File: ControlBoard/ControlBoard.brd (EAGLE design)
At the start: 100 x 80 mm, 7 parts, among them J1 FTDI_DEVICE

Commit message: updates to control board...needs more work
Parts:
- moved R1 112.0 mm to (40.6, 55.9)
- moved C1 105.2 mm to (44.5, 30.5)
- moved J1 104.2 mm to (69.8, 45.7), turned to 270 degrees
- moved R2 100.5 mm to (15.2, 45.7)
- moved S1 100.0 mm to (26.7, 47.0)
- moved X1 73.9 mm to (53.3, 49.5)
- moved JP1 67.1 mm to (33.0, 45.7), turned to 90 degrees
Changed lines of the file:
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@@
 </autorouter>
 <elements>
-<element name="X1" library="adafruit" package="ESP-12" value="" x="-11.43" y="13.97"/>
-<element name="JP1" library="adafruit" package="1X06" value="" x="-7.62" y="-7.62"/>
-<element name="J1" library="quad" package="FTDI_DEVICE_SIDE" value="FTDI_DEVICE" x="-6.35" y="-25.4"/>
-<element name="R1" library="rcl" package="R0603" value="10K" x="-20.32" y="-38.1"/>
-<element name="S1" library="quad" package="TACTILE-SWITCH-SMD" value="SWITCH-MOMENTARY-2SMD" x="-16.51" y="-43.18">
-<attribute name="PROD_ID" value="SWCH-08247" x="-16.51" y="-43.18" size="1.778" layer="27" display="off"/>
+<element name="X1" library="adafruit" package="ESP-12" value="" x="53.34" y="49.53"/>
+<element name="JP1" library="adafruit" package="1X06" value="" x="33.02" y="45.72" rot="R90"/>
+<element name="J1" library="quad" package="FTDI_DEVICE_SIDE" value="FTDI_DEVICE" x="69.85" y="45.72" rot="R270"/>
+<element name="R1" library="rcl" package="R0603" value="10K" x="40.64" y="55.88"/>
+<element name="S1" library="quad" package="TACTILE-SWITCH-SMD" value="SWITCH-MOMENTARY-2SMD" x="26.67" y="46.99">
+<attribute name="PROD_ID" value="SWCH-08247" x="26.67" y="46.99" size="1.778" layer="27" display="off"/>
 </element>
-<element name="R2" library="rcl" package="R0603" value="10K" x="-20.32" y="-48.26"/>
-<element name="C1" library="rcl" package="C0603" value="100nF" x="-19.05" y="-53.34"/>
+<element name="R2" library="rcl" package="R0603" value="10K" x="15.24" y="45.72"/>
+<element name="C1" library="rcl" package="C0603" value="100nF" x="44.45" y="30.48"/>
 </elements>
 <signals>
@@
 <contactref element="JP1" pad="3"/>
 <contactref element="S1" pad="3"/>
-<wire x1="-8.89" y1="-7.62" x2="-19.304" y2="-45.085" width="0" layer="19" extent="1-1"/>
-<wire x1="-3.93" y1="4.47" x2="-8.89" y2="-7.62" width="0" layer="19" extent="1-1"/>
+<wire x1="33.02" y1="44.45" x2="60.84" y2="40.03" width="0" layer="19" extent="1-1"/>
+<wire x1="23.876" y1="45.085" x2="33.02" y2="44.45" width="0" layer="19" extent="1-1"/>
 </signal>
 <signal name="SCK">
 <contactref element="X1" pad="5"/>
 <contactref element="JP1" pad="6"/>
-<wire x1="-1.27" y1="-7.62" x2="-18.93" y2="10.47" width="0" layer="19" extent="1-1"/>
+<wire x1="33.02" y1="52.07" x2="45.84" y2="46.03" width="0" layer="19" extent="1-1"/>
 </signal>
 <signal name="MISO">
 <contactref element="X1" pad="6"/>
 <contactref element="JP1" pad="4"/>
-<wire x1="-18.93" y1="8.47" x2="-6.35" y2="-7.62" width="0" layer="19" extent="1-1"/>
+<wire x1="33.02" y1="46.99" x2="45.84" y2="44.03" width="0" layer="19" extent="1-1"/>
 </signal>
 <signal name="CS">
 <contactref element="X1" pad="12"/>
 <contactref element="JP1" pad="5"/>
-<wire x1="-3.93" y1="10.47" x2="-3.81" y2="-7.62" width="0" layer="19" extent="1-1"/>
+<wire x1="33.02" y1="49.53" x2="60.84" y2="46.03" width="0" layer="19" extent="1-1"/>
 </signal>
 <signal name="TX">
 <contactref element="J1" pad="P$2"/>
 <contactref element="X1" pad="16"/>
-<wire x1="-3.93" y1="18.47" x2="-10.16" y2="-25.4" width="0" layer="19" extent="1-1"/>
+<wire x1="60.84" y1="54.03" x2="69.85" y2="49.53" width="0" layer="19" extent="1-1"/>
 </signal>
 <signal name="RX">
 <contactref element="J1" pad="P$3"/>
 <contactref element="X1" pad="15"/>
-<wire x1="-3.93" y1="16.47" x2="-7.62" y2="-25.4" width="0" layer="19" extent="1-1"/>
+<wire x1="60.84" y1="52.03" x2="69.85" y2="46.99" width="0" layer="19" extent="1-1"/>
 </signal>
 <signal name="N$1">
 <contactref element="J1" pad="P$5"/>
 <contactref element="J1" pad="P$6"/>
-<wire x1="0" y1="-25.4" x2="-2.54" y2="-25.4" width="0" layer="19" extent="1-1"/>
+<wire x1="69.85" y1="39.37" x2="69.85" y2="41.91" width="0" layer="19" extent="1-1"/>
 </signal>
 <signal name="DTR">
 <contactref element="J1" pad="P$1"/>
 <contactref element="C1" pad="2"/>
-<wire x1="-12.7" y1="-25.4" x2="-18.2" y2="-53.34" width="0" layer="19" extent="1-1"/>
+<wire x1="45.3" y1="30.48" x2="69.85" y2="52.07" width="0" layer="19" extent="1-1"/>
 </signal>
 <signal name="3V3">
@@
 <contactref element="JP1" pad="1"/>
 <contactref element="R2" pad="2"/>
-<wire x1="-21.17" y1="-38.1" x2="-19.47" y2="-48.26" width="0" layer="19" extent="1-1"/>
-<wire x1="-5.08" y1="-25.4" x2="-21.17" y2="-38.1" width="0" layer="19" extent="1-1"/>
-<wire x1="-13.97" y1="-7.62" x2="-5.08" y2="-25.4" width="0" layer="19" extent="1-1"/>
-<wire x1="-18.93" y1="4.47" x2="-13.97" y2="-7.62" width="0" layer="19" extent="1-1"/>
+<wire x1="45.84" y1="40.03" x2="69.85" y2="44.45" width="0" layer="19" extent="1-1"/>
+<wire x1="33.02" y1="39.37" x2="45.84" y2="40.03" width="0" layer="19" extent="1-1"/>
+<wire x1="39.79" y1="55.88" x2="45.84" y2="40.03" width="0" layer="19" extent="1-1"/>
+<wire x1="16.09" y1="45.72" x2="33.02" y2="39.37" width="0" layer="19" extent="1-1"/>
 </signal>
 <signal name="CH_PD">
 <contactref element="R1" pad="2"/>
 <contactref element="X1" pad="3"/>
-<wire x1="-18.93" y1="14.47" x2="-19.47" y2="-38.1" width="0" layer="19" extent="1-1"/>
+<wire x1="45.84" y1="50.03" x2="41.49" y2="55.88" width="0" layer="19" extent="1-1"/>
 </signal>
 <signal name="RST">
@@
 <contactref element="R2" pad="1"/>
 <contactref element="C1" pad="1"/>
-<wire x1="-21.17" y1="-48.26" x2="-19.9" y2="-53.34" width="0" layer="19" extent="1-1"/>
-<wire x1="-19.304" y1="-41.275" x2="-21.17" y2="-48.26" width="0" layer="19" extent="1-1"/>
-<wire x1="-18.93" y1="18.47" x2="-19.304" y2="-41.275" width="0" layer="19" extent="1-1"/>
+<wire x1="23.876" y1="48.895" x2="45.84" y2="54.03" width="0" layer="19" extent="1-1"/>
+<wire x1="14.39" y1="45.72" x2="23.876" y2="48.895" width="0" layer="19" extent="1-1"/>
+<wire x1="43.6" y1="30.48" x2="45.84" y2="54.03" width="0" layer="19" extent="1-1"/>
 </signal>
 </signals>

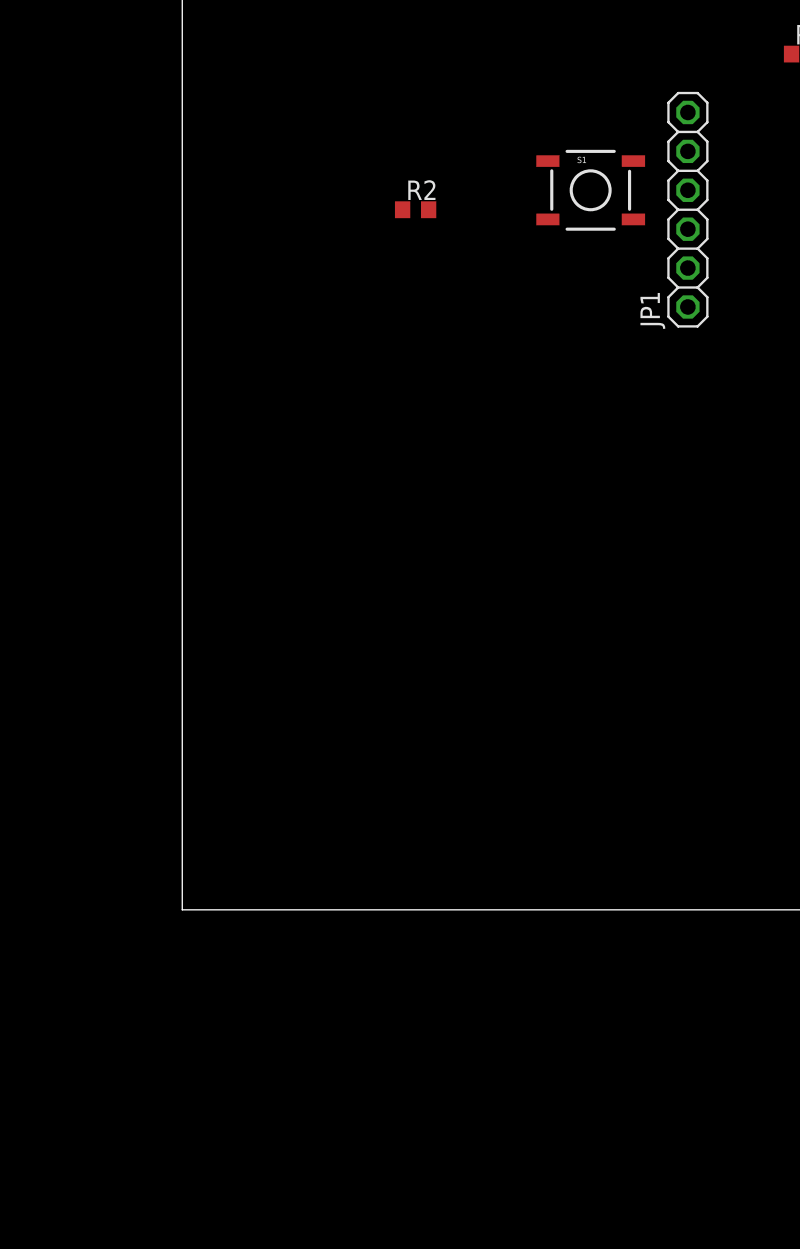
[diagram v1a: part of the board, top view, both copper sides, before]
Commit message: added thermocouple-digital chip
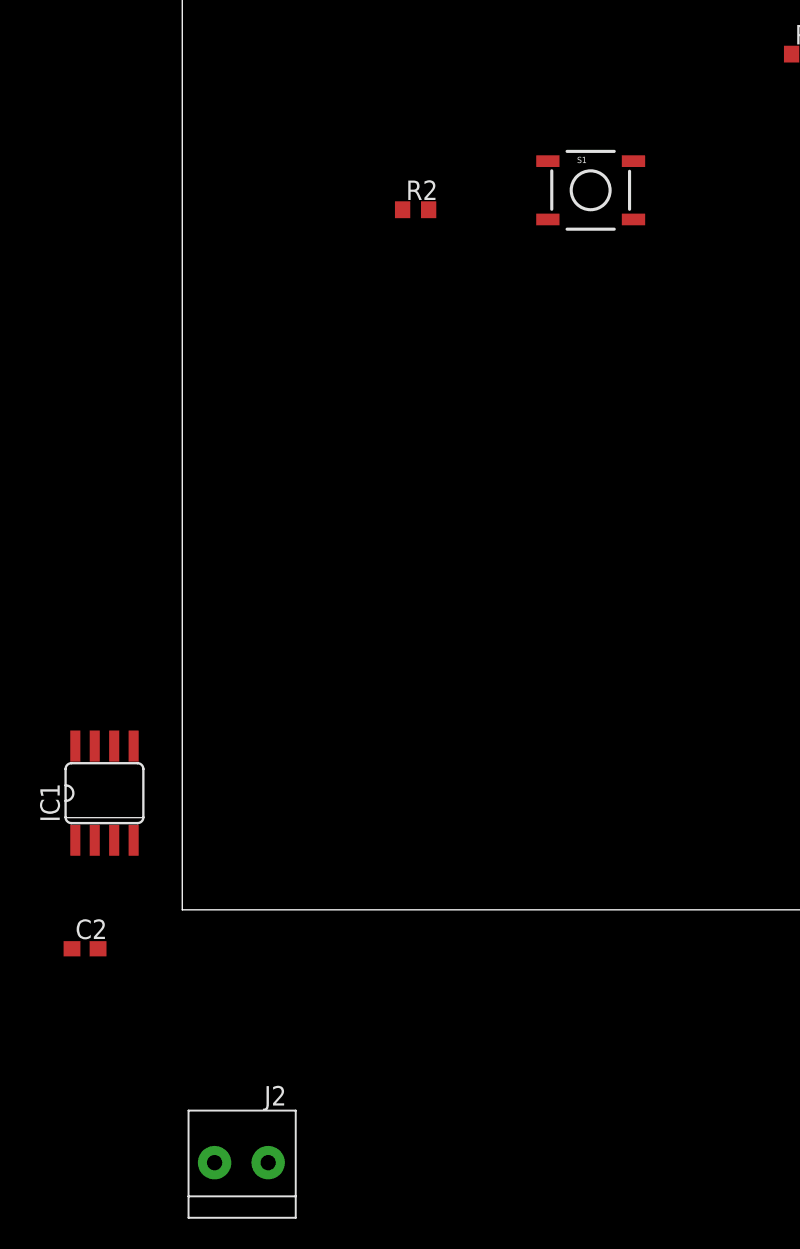
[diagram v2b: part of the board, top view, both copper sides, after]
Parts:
- removed JP1: (no value), adafruit:1X06
- added C2: 100nF, rcl:C0603
- added IC1: MAX6675, adafruit:SO08
- added J2: 1X2-3.5MM, adafruit:1X2-3.5MM
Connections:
- new net T+: C2.1, IC1.3, J2.1
- new net T-: C2.2, IC1.2, J2.2
- net 3V3: now also IC1.4; no longer JP1.1
- net CS: now also IC1.6; no longer JP1.5
- net GND: now also IC1.1; no longer JP1.3
- net MISO: now also IC1.7; no longer JP1.4
- net SCK: now also IC1.5; no longer JP1.6
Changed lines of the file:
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@@
 <elements>
 <element name="X1" library="adafruit" package="ESP-12" value="" x="53.34" y="49.53"/>
-<element name="JP1" library="adafruit" package="1X06" value="" x="33.02" y="45.72" rot="R90"/>
 <element name="J1" library="quad" package="FTDI_DEVICE_SIDE" value="FTDI_DEVICE" x="69.85" y="45.72" rot="R270"/>
 <element name="R1" library="rcl" package="R0603" value="10K" x="40.64" y="55.88"/>
@@
 <element name="R2" library="rcl" package="R0603" value="10K" x="15.24" y="45.72"/>
 <element name="C1" library="rcl" package="C0603" value="100nF" x="44.45" y="30.48"/>
+<element name="IC1" library="adafruit" package="SO08" value="MAX6675" x="-5.08" y="7.62"/>
+<element name="C2" library="rcl" package="C0603" value="100nF" x="-6.35" y="-2.54"/>
+<element name="J2" library="adafruit" package="1X2-3.5MM" value="1X2-3.5MM" x="3.81" y="-16.51"/>
 </elements>
 <signals>
 <signal name="GND">
 <contactref element="X1" pad="9"/>
-<contactref element="JP1" pad="3"/>
 <contactref element="S1" pad="3"/>
-<wire x1="33.02" y1="44.45" x2="60.84" y2="40.03" width="0" layer="19" extent="1-1"/>
-<wire x1="23.876" y1="45.085" x2="33.02" y2="44.45" width="0" layer="19" extent="1-1"/>
+<contactref element="IC1" pad="1"/>
+<wire x1="23.876" y1="45.085" x2="60.84" y2="40.03" width="0" layer="19" extent="1-1"/>
+<wire x1="-6.985" y1="4.5466" x2="23.876" y2="45.085" width="0" layer="19" extent="1-1"/>
 </signal>
 <signal name="SCK">
 <contactref element="X1" pad="5"/>
-<contactref element="JP1" pad="6"/>
-<wire x1="33.02" y1="52.07" x2="45.84" y2="46.03" width="0" layer="19" extent="1-1"/>
+<contactref element="IC1" pad="5"/>
+<wire x1="-3.175" y1="10.6934" x2="45.84" y2="46.03" width="0" layer="19" extent="1-1"/>
 </signal>
 <signal name="MISO">
 <contactref element="X1" pad="6"/>
-<contactref element="JP1" pad="4"/>
-<wire x1="33.02" y1="46.99" x2="45.84" y2="44.03" width="0" layer="19" extent="1-1"/>
+<contactref element="IC1" pad="7"/>
+<wire x1="-5.715" y1="10.6934" x2="45.84" y2="44.03" width="0" layer="19" extent="1-1"/>
 </signal>
 <signal name="CS">
 <contactref element="X1" pad="12"/>
-<contactref element="JP1" pad="5"/>
-<wire x1="33.02" y1="49.53" x2="60.84" y2="46.03" width="0" layer="19" extent="1-1"/>
+<contactref element="IC1" pad="6"/>
+<wire x1="-4.445" y1="10.6934" x2="60.84" y2="46.03" width="0" layer="19" extent="1-1"/>
 </signal>
 <signal name="TX">
@@
 <contactref element="X1" pad="8"/>
 <contactref element="R1" pad="1"/>
-<contactref element="JP1" pad="1"/>
 <contactref element="R2" pad="2"/>
+<contactref element="IC1" pad="4"/>
 <wire x1="45.84" y1="40.03" x2="69.85" y2="44.45" width="0" layer="19" extent="1-1"/>
-<wire x1="33.02" y1="39.37" x2="45.84" y2="40.03" width="0" layer="19" extent="1-1"/>
 <wire x1="39.79" y1="55.88" x2="45.84" y2="40.03" width="0" layer="19" extent="1-1"/>
-<wire x1="16.09" y1="45.72" x2="33.02" y2="39.37" width="0" layer="19" extent="1-1"/>
+<wire x1="16.09" y1="45.72" x2="39.79" y2="55.88" width="0" layer="19" extent="1-1"/>
+<wire x1="-3.175" y1="4.5466" x2="16.09" y2="45.72" width="0" layer="19" extent="1-1"/>
 </signal>
 <signal name="CH_PD">
@@
 <wire x1="43.6" y1="30.48" x2="45.84" y2="54.03" width="0" layer="19" extent="1-1"/>
 </signal>
+<signal name="T-">
+<contactref element="C2" pad="2"/>
+<contactref element="IC1" pad="2"/>
+<contactref element="J2" pad="2"/>
+<wire x1="-5.5" y1="-2.54" x2="2.11" y2="-16.51" width="0" layer="19" extent="1-1"/>
+<wire x1="-5.715" y1="4.5466" x2="-5.5" y2="-2.54" width="0" layer="19" extent="1-1"/>
+</signal>
+<signal name="T+">
+<contactref element="IC1" pad="3"/>
+<contactref element="C2" pad="1"/>
+<contactref element="J2" pad="1"/>
+<wire x1="-7.2" y1="-2.54" x2="5.61" y2="-16.51" width="0" layer="19" extent="1-1"/>
+<wire x1="-4.445" y1="4.5466" x2="-7.2" y2="-2.54" width="0" layer="19" extent="1-1"/>
+</signal>
 </signals>

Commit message: updated eagle board and schematic files
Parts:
- added C3, C4: 1uF, rcl:C0603
- added J3: 1X2-3.5MM, adafruit:1X2-3.5MM
- added MCP1802T-3302I/OT: (no value), quad:SOT95P270X145-5N
- added T1: 2N4401, transistor:TO92-EBC
- added X2: MINI-USB-32005-201, con-cypressindustries:32005-201
- moved R1 47.3 mm to (19.7, 13.5)
- moved J1 44.6 mm to (42.8, 10.2)
- moved X1 43.1 mm to (30.5, 13.0)
- moved S1 35.0 mm to (13.9, 14.4), turned to 180 degrees
- moved R2 30.0 mm to (19.7, 16.0), turned to 180 degrees
- moved C1 26.5 mm to (20.7, 18.8), turned to 90 degrees
- moved J2 24.0 mm to (6.38, 7.39), turned to 270 degrees
- moved IC1 19.4 mm to (14.3, 7.42), turned to 270 degrees
- moved C2 18.0 mm to (8.71, 7.37), flipped to the bottom, turned to 90 degrees
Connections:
- net T+ renamed THERMOCOUPLE+
- net T- renamed THERMOCOUPLE-
- removed net N$1: J1.P$5, J1.P$6
- new net 5V: C3.1, MCP1802T-3302I/OT.1, MCP1802T-3302I/OT.3, T1.C, X2.1
- new net CTS: J1.P$5, X1.7
- new net RELAY_COIL: J3.1, T1.E
- new net RELAY_CTRL: T1.B, X1.14
- net 3V3: now also C4.1, MCP1802T-3302I/OT.5
- net CS: now also X1.10; no longer X1.12
- net GND: now also C3.2, C4.2, J1.P$6, J3.2, MCP1802T-3302I/OT.2, X2.5
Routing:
- net GND: track 0.00 -> 42.8 mm, vias 0 -> 1
- net RELAY_CTRL: track 0.00 -> 36.3 mm
- net 5V: track 0.00 -> 30.3 mm
- net DTR: track 0.00 -> 23.4 mm
- net CS: track 0.00 -> 21.2 mm
- net CTS: track 0.00 -> 21.0 mm
- net SCK: track 0.00 -> 13.8 mm
- net RELAY_COIL: track 0.00 -> 11.2 mm
- net RST: track 0.00 -> 10.6 mm
- net THERMOCOUPLE+: track 0.00 -> 8.04 mm
- net THERMOCOUPLE-: track 0.00 -> 7.96 mm
- net RX: track 0.00 -> 7.74 mm
- net TX: track 0.00 -> 7.00 mm
- net MISO: track 0.00 -> 5.92 mm
- net CH_PD: track 0.00 -> 2.45 mm
- added copper zone on layer 1, net 3V3
- added copper zone on layer 16, net GND
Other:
- board size 100 x 80 mm -> 50 x 40 mm
